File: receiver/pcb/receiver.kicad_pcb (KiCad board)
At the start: 2 copper layers, 39 x 43.2 mm, 23 parts, among them M1 Conn_01x02_Female, M2 Conn_01x02_Female, U1 DRV8870DDA, U2 DRV8870DDA

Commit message: V3 of receiver as ordered.
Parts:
- removed the R2 at (176.5, 109.0)
- added R1: 10k, Resistor_SMD:R_0805_2012Metric_Pad1.20x1.40mm_HandSolder, F.Cu at (178.4, 108.6)
- AMS1117: moved to B.Cu
- Batt1: footprint Connector_PinSocket_2.54mm:PinSocket_1x02_P2.54mm_Vertical -> battery:battery_pads
- moved AMS1117 5.71 mm to (160.4, 87.6)
- moved Batt1 4.03 mm to (167.9, 82.5)
- moved H3 2.83 mm to (182.8, 83.0)
- moved G*** 2.74 mm to (163.8, 98.4)
- moved H1 2.00 mm to (150.8, 83.0)
- moved H4 2.00 mm to (182.8, 115.0)
- moved BZ1 0.70 mm to (171.5, 114.3)
- renumbered PWR1 to LED1, R680 to R2
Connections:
- ESC1 pad 1: Net-(ESC1-Pad1) -> Net-(ESC1-Pin_1)
- ESP32-C3 pad 19: Net-(ESP32-C3-Pad19) -> Net-(ESC1-Pin_1)
- Servo1 pad 1: +6V -> /Servo
- Servo1 pad 2: /Servo -> +6V
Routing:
- net Net-(ESC1-Pin_1): track 0.00 -> 22.5 mm
- net +12V: track 101.0 -> 87.1 mm
- net Net-(ESP32-C3-Pad19): track 13.4 -> 0.00 mm
- net Net-(ESC1-Pad1): track 7.90 -> 0.00 mm
- net GND: track 141.6 -> 133.7 mm, vias 1 -> 2
- net /Servo: track 34.5 -> 31.7 mm
- net +3V3: track 79.5 -> 81.9 mm, vias 3 -> 4
- net /spkr: track 13.7 -> 13.0 mm
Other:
- board size 39 x 43.2 mm -> 41 x 41 mm
- board text added: "32x32mm mounting holes"
- board text added: "S"
- board text added: "VS Receiver V3"
- board text removed: "6V"
- board text removed: "Sig"
- board text removed: "VS Receiver ESP32-C3 Rev1"

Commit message: updated motor labels on receiver and added receiver schematic pdf
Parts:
- renumbered M1 to LM, M2 to RM
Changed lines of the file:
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@@
     (property "ki_keywords" "connector")
     (attr through_hole)
-    (fp_text reference "M1" (at -2.5 1.27 90) (layer "F.SilkS")
+    (fp_text reference "LM" (at -2.5 1.27 90) (layer "F.SilkS")
         (effects (font (size 1 1) (thickness 0.15)))
     )
@@
     (property "ki_keywords" "connector")
     (attr through_hole)
-    (fp_text reference "M2" (at -2.5 1.25 90) (layer "F.SilkS")
+    (fp_text reference "RM" (at -2.5 1.25 90) (layer "F.SilkS")
         (effects (font (size 1 1) (thickness 0.15)))
     )

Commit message: receiver V4 ordered
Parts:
- removed AMS1117: AMS1117-3.3, Package_TO_SOT_SMD:SOT-223-3_TabPin2
- removed BZ1: Buzzer, Buzzer_Beeper:Buzzer_CUI_CPT-9019S-SMT
- added Comms1: LED, LED_SMD:LED_0805_2012Metric_Pad1.15x1.40mm_HandSolder, F.Cu at (176.0, 116.8)
- added PS1: UA78M33CDCYRG3, ua78-vreg:SOT230P700X180-4N, B.Cu at (160.5, 87.5)
- added R3: 680 ohm, Resistor_SMD:R_0805_2012Metric_Pad1.20x1.40mm_HandSolder, F.Cu at (176.0, 112.1)
- moved R2 15.5 mm to (171.4, 112.0), turned to -90 degrees
- moved PWR1 12.4 mm to (171.4, 116.8), turned to 90 degrees
- moved Batt1 7.18 mm to (175.0, 81.8), turned to -90 degrees
- moved ML 2.04 mm to (183.6, 99.2)
- moved MR 1.89 mm to (183.6, 91.7)
- renumbered LM to ML, RM to MR, LED1 to PWR1
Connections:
- ESP32-C3 pad 18: /spkr -> /pwr
- ESP32-C3 pad 20: unconnected-(ESP32-C3-GPIO6-Pad20) -> /comms
- R2 pad 1: +3V3 -> /pwr
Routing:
- net +12V: track 87.1 -> 123.6 mm
- net +3V3: track 81.9 -> 51.2 mm
- net /spkr: track 13.0 -> 0.00 mm
- net /pwr: track 0.00 -> 12.8 mm
- net /comms: track 0.00 -> 12.3 mm
- net GND: track 133.7 -> 141.9 mm
- net +6V: track 13.2 -> 10.4 mm, vias 1 -> 0
- net Net-(Comms1-A): track 0.00 -> 2.74 mm
- net Net-(ESC1-Pin_1): track 22.5 -> 25.2 mm
- net Net-(ML1-Pin_2): track 5.14 -> 7.35 mm
- net Net-(MR1-Pin_2): track 5.14 -> 7.14 mm
- net Net-(MR1-Pin_1): track 5.14 -> 6.98 mm
- net Net-(ML1-Pin_1): track 5.14 -> 6.93 mm
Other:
- board text added: "VS Receiver V4"
- board text removed: "GND"
- board text removed: "VS Receiver V3"

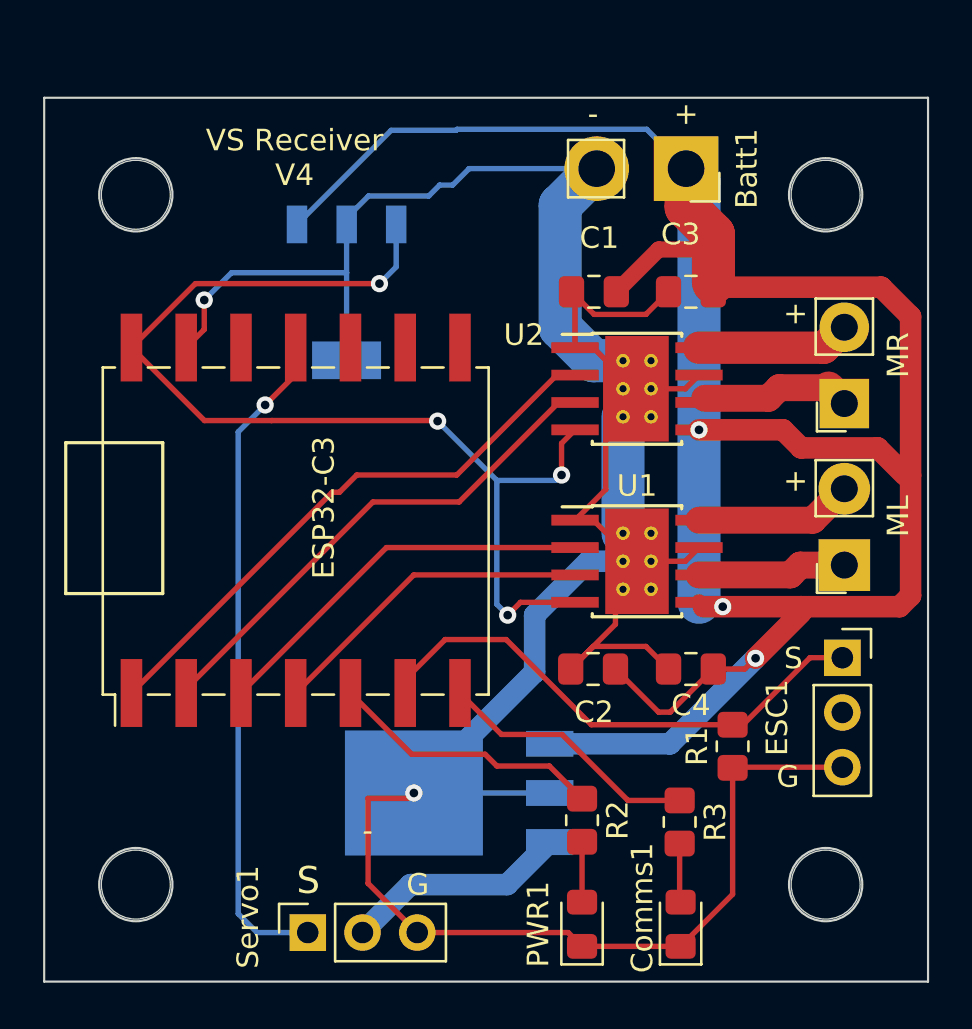
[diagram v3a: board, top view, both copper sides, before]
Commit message: Receiver V5 as ordered.
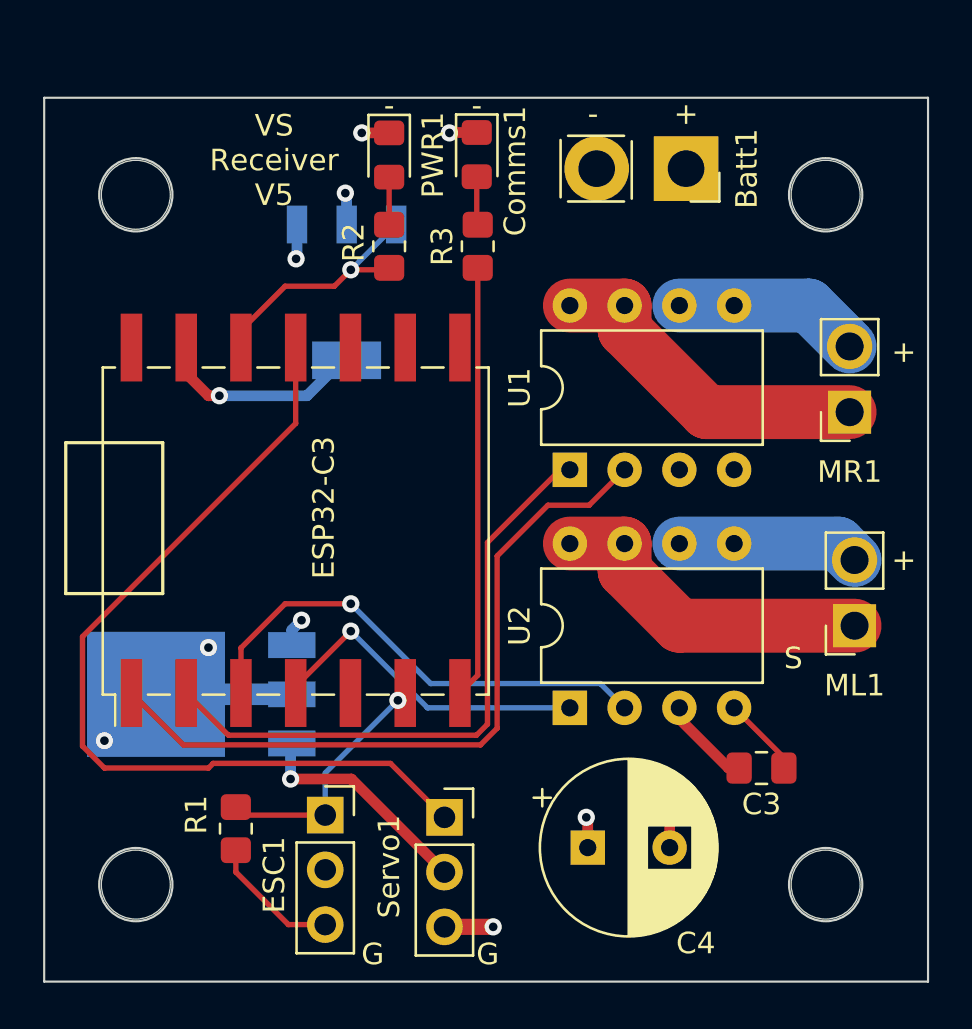
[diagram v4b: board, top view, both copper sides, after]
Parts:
- removed C1: .1 uF, Capacitor_SMD:C_0805_2012Metric_Pad1.18x1.45mm_HandSolder
- removed C2: 0.1 uF, Capacitor_SMD:C_0805_2012Metric_Pad1.18x1.45mm_HandSolder
- removed the G*** at (163.8, 98.4)
- removed ML, MR: Conn_01x02_Female, Connector_PinSocket_2.54mm:PinSocket_1x02_P2.54mm_Vertical
- added G***: LOGO, VS-Logo:VS-Logo_small, B.Cu at (161.0, 97.1)
- added ML1: Conn_01x02_Female, custom:DC_motor_output, F.Cu at (184.1, 103.0)
- added MR1: Conn_01x02_Female, custom:DC_motor_output, F.Cu at (183.9, 93.1)
- C3: value 47 uF -> .1 uF
- C4: value 47uF -> 470 uF; footprint Capacitor_SMD:C_0805_2012Metric_Pad1.18x1.45mm_HandSolder -> Capacitor_THT:CP_Radial_D8.0mm_P3.80mm
- U1, U2: value DRV8870DDA -> RZ7886; footprint Package_SO:Texas_HTSOP-8-1EP_3.9x4.9mm_P1.27mm_EP2.95x4.9mm_Mask2.4x3.1mm_ThermalVias -> Package_DIP:DIP-8_W7.62mm
- moved Comms1 36.9 mm to (166.6, 81.1), turned to -90 degrees
- moved PWR1 36.8 mm to (162.5, 81.2), turned to -90 degrees
- moved R3 28.3 mm to (166.6, 85.4), turned to 90 degrees
- moved R2 28.1 mm to (162.5, 85.4), turned to 90 degrees
- moved ESC1 25.1 mm to (159.5, 111.8)
- moved R1 23.4 mm to (155.4, 112.4)
- moved C3 22.3 mm to (179.8, 109.6)
- moved U2 15.1 mm to (170.9, 106.8), turned to 90 degrees
- moved L7806 12.8 mm to (153.8, 106.2)
- moved C4 9.57 mm to (171.7, 113.3), turned to 0 degrees
- moved Servo1 8.29 mm to (165.1, 111.9), turned to 0 degrees
- moved U1 5.26 mm to (170.9, 95.8), turned to 90 degrees
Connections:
- ESP32-C3 pad 18: /pwr -> unconnected-(ESP32-C3-GPIO4/ADC1_CH4-Pad18)
- R2 pad 1: /pwr -> +3V3
- U1 pad 1: GND -> Net-(ESP32-C3-GPIO1/ADC1_CH1/XTAL_32K_N)
- U1 pad 2: Net-(ESP32-C3-GPIO2/ADC1_CH2) -> Net-(ESP32-C3-GPIO0/ADC1_CH0/XTAL_32K_P)
- U1 pad 3: Net-(ESP32-C3-GPIO3/ADC1_CH3) -> GND
- U1 pad 4: +3V3 -> +12V
- U1 pad 5: +12V -> Net-(MR1-Pin_2)
- U1 pad 6: Net-(ML1-Pin_1) -> Net-(MR1-Pin_2)
- U1 pad 7: GND -> Net-(MR1-Pin_1)
- U1 pad 8: Net-(ML1-Pin_2) -> Net-(MR1-Pin_1)
- U2 pad 1: GND -> Net-(ESP32-C3-GPIO3/ADC1_CH3)
- U2 pad 2: Net-(ESP32-C3-GPIO0/ADC1_CH0/XTAL_32K_P) -> Net-(ESP32-C3-GPIO2/ADC1_CH2)
- U2 pad 3: Net-(ESP32-C3-GPIO1/ADC1_CH1/XTAL_32K_N) -> GND
- U2 pad 4: +3V3 -> +12V
- U2 pad 5: +12V -> Net-(ML1-Pin_2)
- U2 pad 6: Net-(MR1-Pin_1) -> Net-(ML1-Pin_2)
- U2 pad 7: GND -> Net-(ML1-Pin_1)
- U2 pad 8: Net-(MR1-Pin_2) -> Net-(ML1-Pin_1)
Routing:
- net +12V: track 123.6 -> 8.14 mm
- net GND: track 141.9 -> 34.4 mm, vias 2 -> 8
- net +3V3: track 51.2 -> 11.8 mm, vias 4 -> 1
- net Net-(ESC1-Pin_1): track 25.2 -> 11.0 mm, vias 0 -> 1
- net /pwr: track 12.8 -> 0.00 mm
- net /Servo: track 31.7 -> 40.9 mm, vias 1 -> 0
- net Net-(MR1-Pin_1): track 6.98 -> 15.7 mm
- net Net-(ML1-Pin_1): track 6.93 -> 15.5 mm
- net /comms: track 12.3 -> 20.1 mm
- net Net-(ESP32-C3-GPIO0/ADC1_CH0/XTAL_32K_P): track 26.7 -> 33.8 mm
- net Net-(ESP32-C3-GPIO1/ADC1_CH1/XTAL_32K_N): track 23.7 -> 28.6 mm
- net Net-(ESP32-C3-GPIO2/ADC1_CH2): track 18.3 -> 22.7 mm, vias 0 -> 1
- net Net-(MR1-Pin_2): track 7.14 -> 8.69 mm
- net Net-(ML1-Pin_2): track 7.35 -> 8.44 mm
- net Net-(PWR1-A): track 2.80 -> 2.21 mm
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- added copper zone on In1.Cu, net +12V
- added copper zone on In2.Cu, net GND
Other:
- copper layers 2 -> 4
- board text added: "VS Receiver V5"
- board text removed: "VS Receiver V4"
